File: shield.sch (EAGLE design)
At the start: 31 parts, among them Q1 PMV20EN, Q2 PMV20EN, Q3 PMV20EN, Q4 PMV20EN, Q5 PMV20EN, Q6 PMV20EN, U1 ATMEGA168

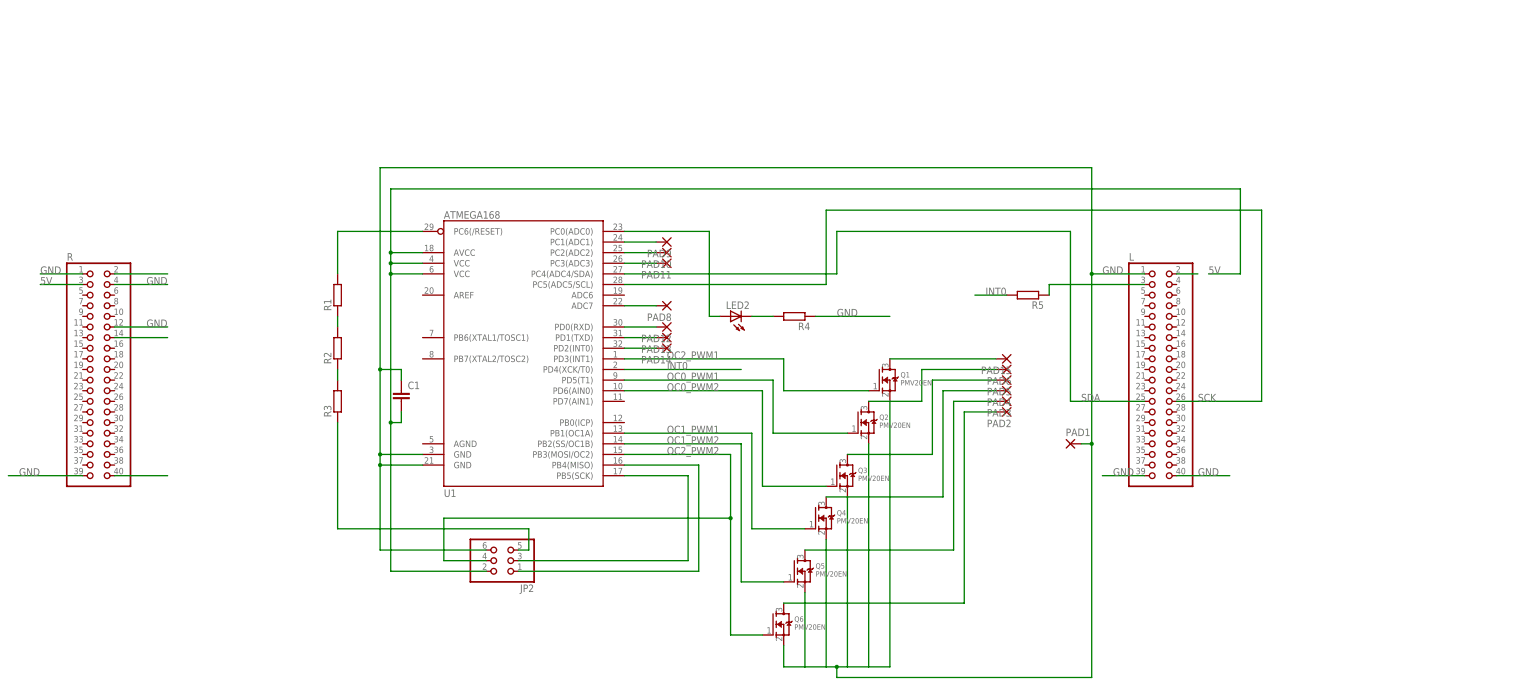
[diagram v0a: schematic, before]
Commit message: added 3.3/5V, a chargin pin and fixed chip layout
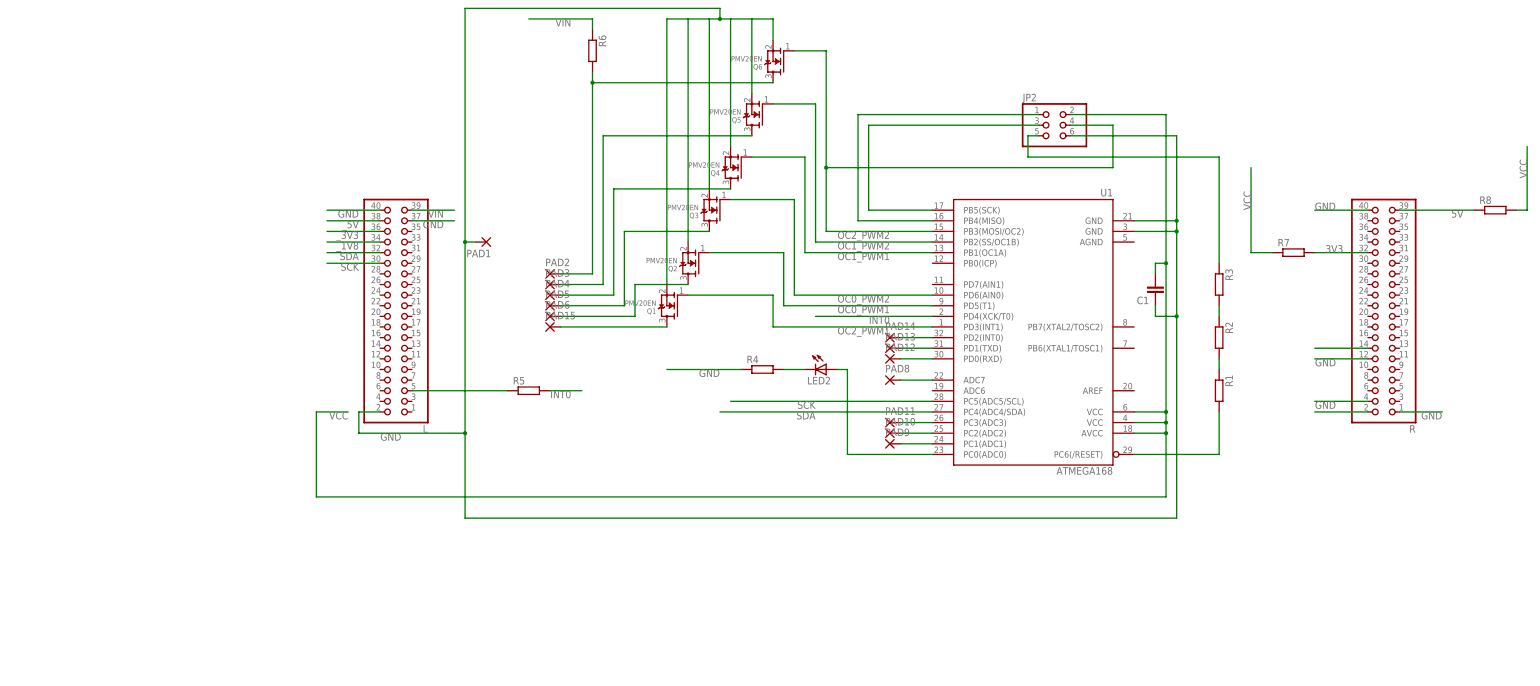
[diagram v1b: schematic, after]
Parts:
- added R6: (no value), rcl:R-EU_M1206
- added R7, R8: (no value), rcl:R-EU_M0805
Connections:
- removed net N$20: R.40
- removed net N$22: L.2
- new net 3V3: R.32, R7.2
- new net VCC: C1.2, JP2.2, R7.1, R8.2, U1.AVCC, U1.VCC@1, U1.VCC@2
- new net VIN: L.39, R6.1
- new net _1V8: L.34
- new net _3V3: L.36
- new net _5V: L.38
- net 5V: now also R.39, R8.1; no longer C1.2, JP2.2, R.3, U1.AVCC, U1.VCC@1, U1.VCC@2
- net GND: now also L.2, L.37, R.40, U1.GND@2; no longer L.1, L.39, R.39
- net N$25: now also L.5; no longer L.3
- net N$9: now also R6.2
- net SCK: now also L.30; no longer L.26
- net SDA: now also L.32; no longer L.25
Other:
- moved on the sheet: C1, JP2, L, LED2, PAD1, PAD10, PAD11, PAD12, PAD13, PAD14, PAD15, PAD2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
